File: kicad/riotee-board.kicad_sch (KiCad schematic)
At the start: 0 parts

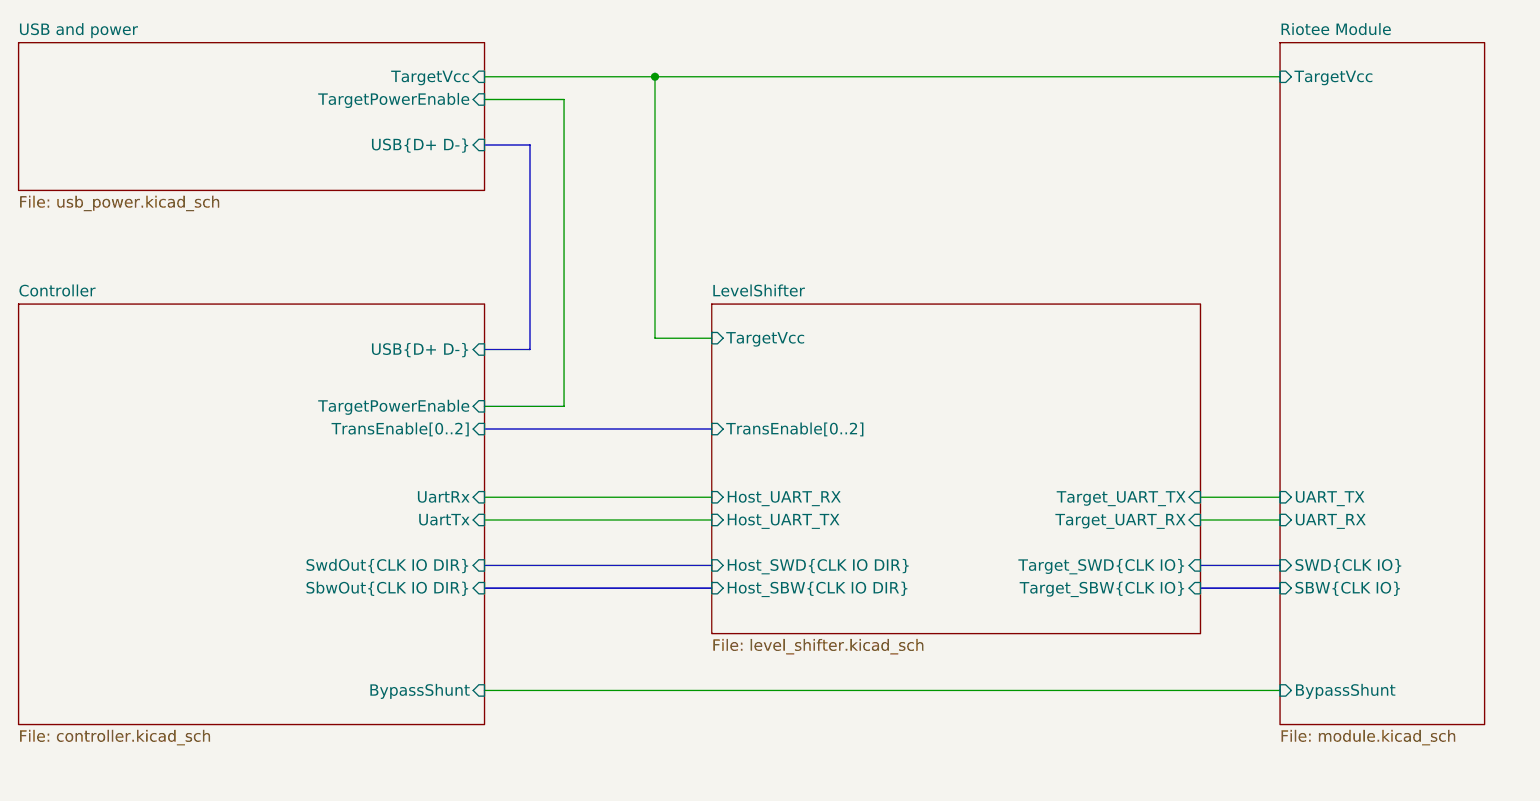
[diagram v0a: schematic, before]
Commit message: add fourth level converter for simultaneous programming + TX/RX
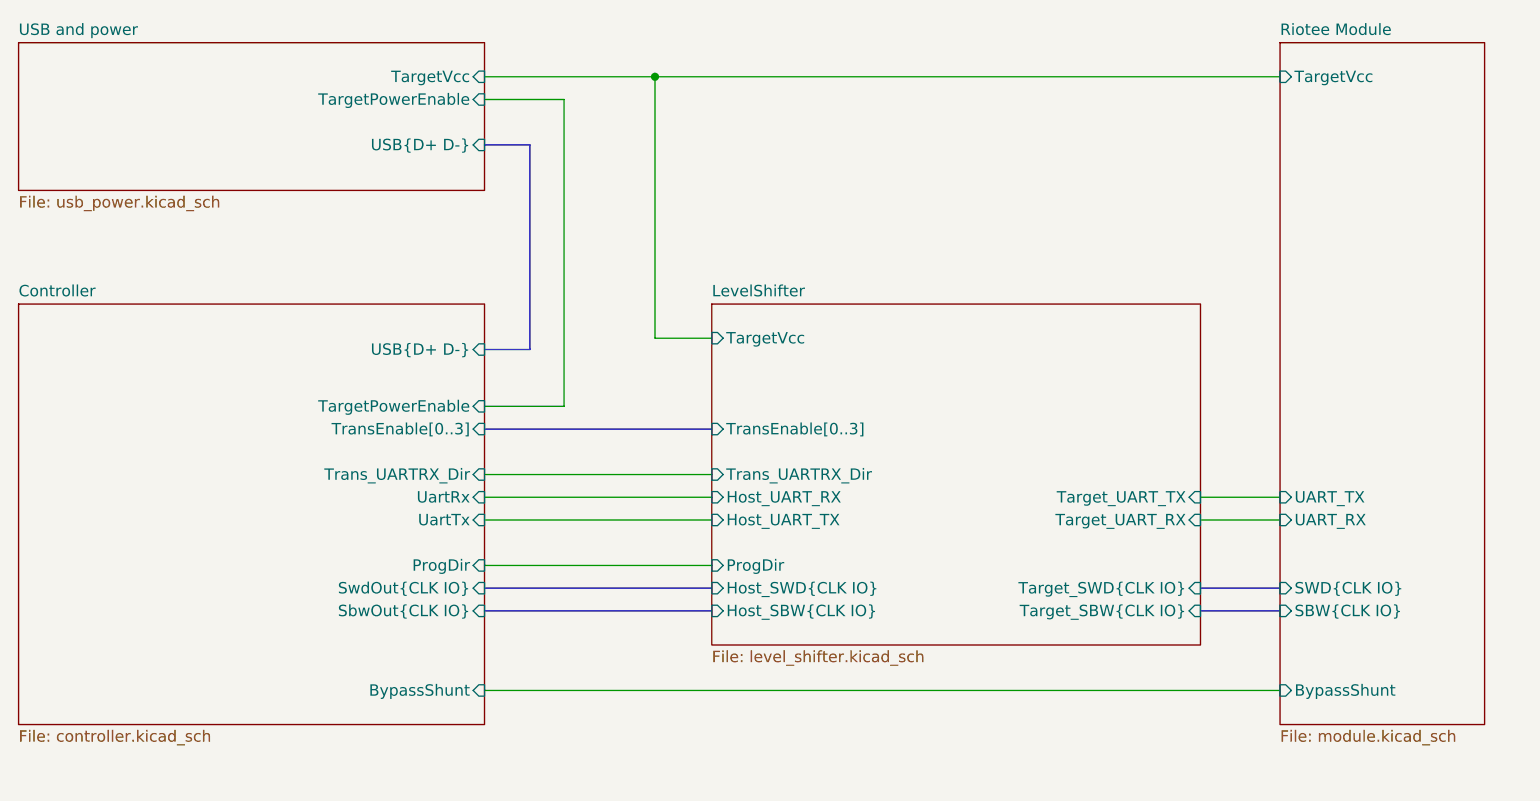
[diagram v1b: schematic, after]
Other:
- sheet Controller ports: added ProgDir, SbwOut{CLK IO}, SwdOut{CLK IO}, TransEnable[0..3], Trans_UARTRX_Dir; removed SbwOut{CLK IO DIR}, SwdOut{CLK IO DIR}, TransEnable[0..2]
- sheet LevelShifter ports: added Host_SBW{CLK IO}, Host_SWD{CLK IO}, ProgDir, TransEnable[0..3], Trans_UARTRX_Dir; removed Host_SBW{CLK IO DIR}, Host_SWD{CLK IO DIR}, TransEnable[0..2]

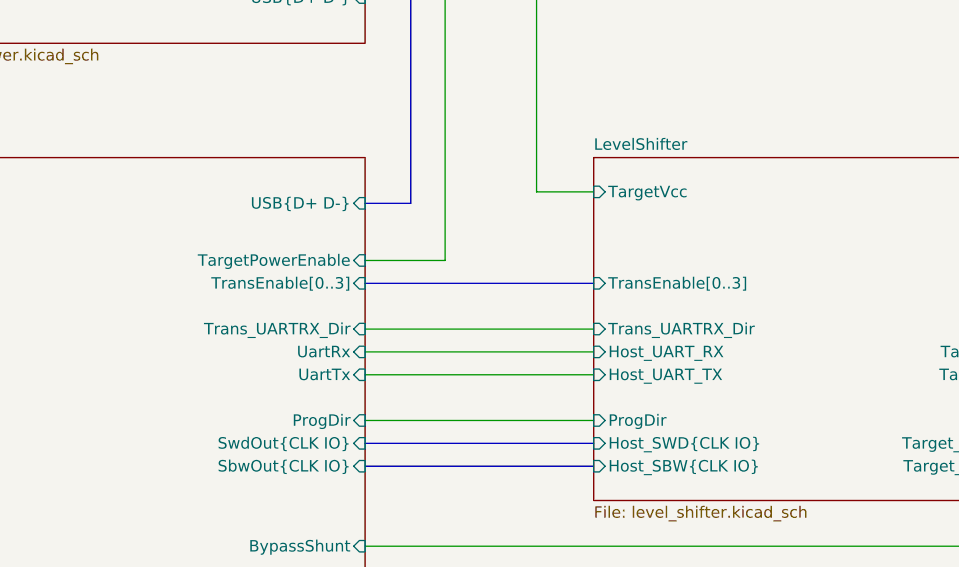
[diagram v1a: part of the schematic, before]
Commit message: fix some net names
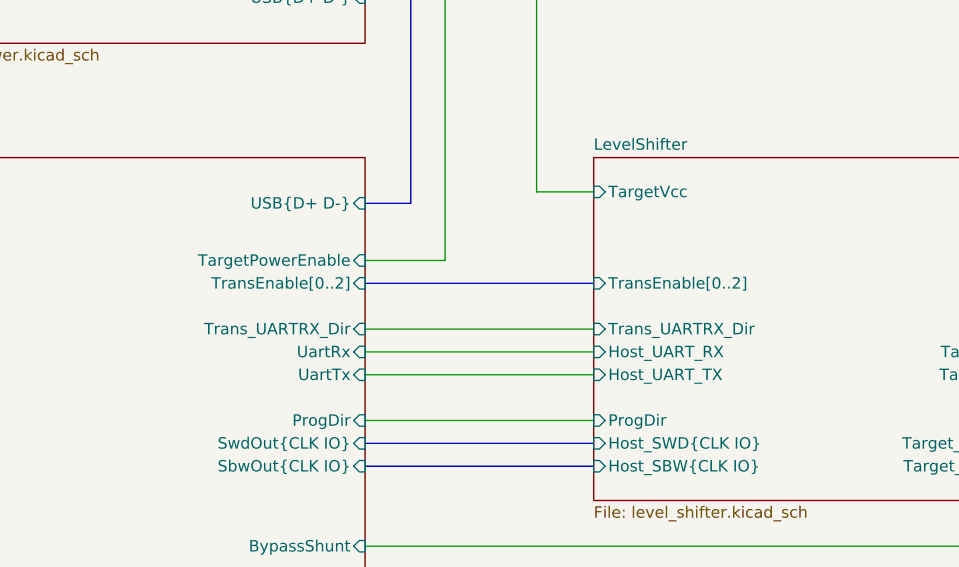
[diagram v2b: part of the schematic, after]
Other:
- sheet Controller ports: added TransEnable[0..2]; removed TransEnable[0..3]
- sheet LevelShifter ports: added TransEnable[0..2]; removed TransEnable[0..3]
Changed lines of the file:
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@@
       (effects (font (size 1.27 1.27)) (justify right))
     )
-    (pin "TransEnable[0..3]" input (at 114.3 104.14 0)
+    (pin "TransEnable[0..2]" input (at 114.3 104.14 0)
       (effects (font (size 1.27 1.27)) (justify right))
     )
@@
       (effects (font (size 1.27 1.27)) (justify left))
     )
-    (pin "TransEnable[0..3]" input (at 139.7 104.14 180)
+    (pin "TransEnable[0..2]" input (at 139.7 104.14 180)
       (effects (font (size 1.27 1.27)) (justify left))
     )

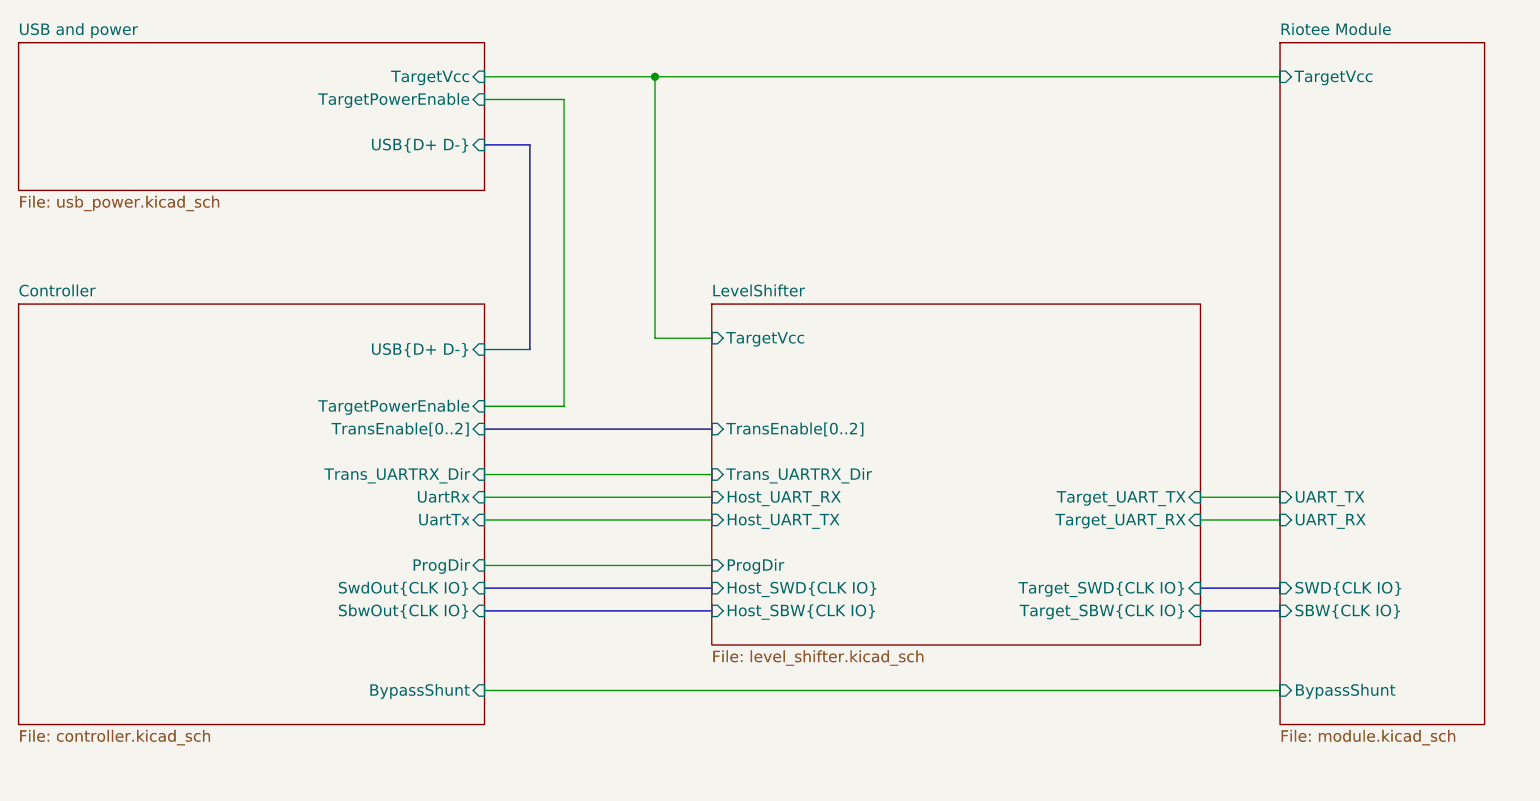
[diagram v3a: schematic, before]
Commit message: replace target supply diode with analog switch
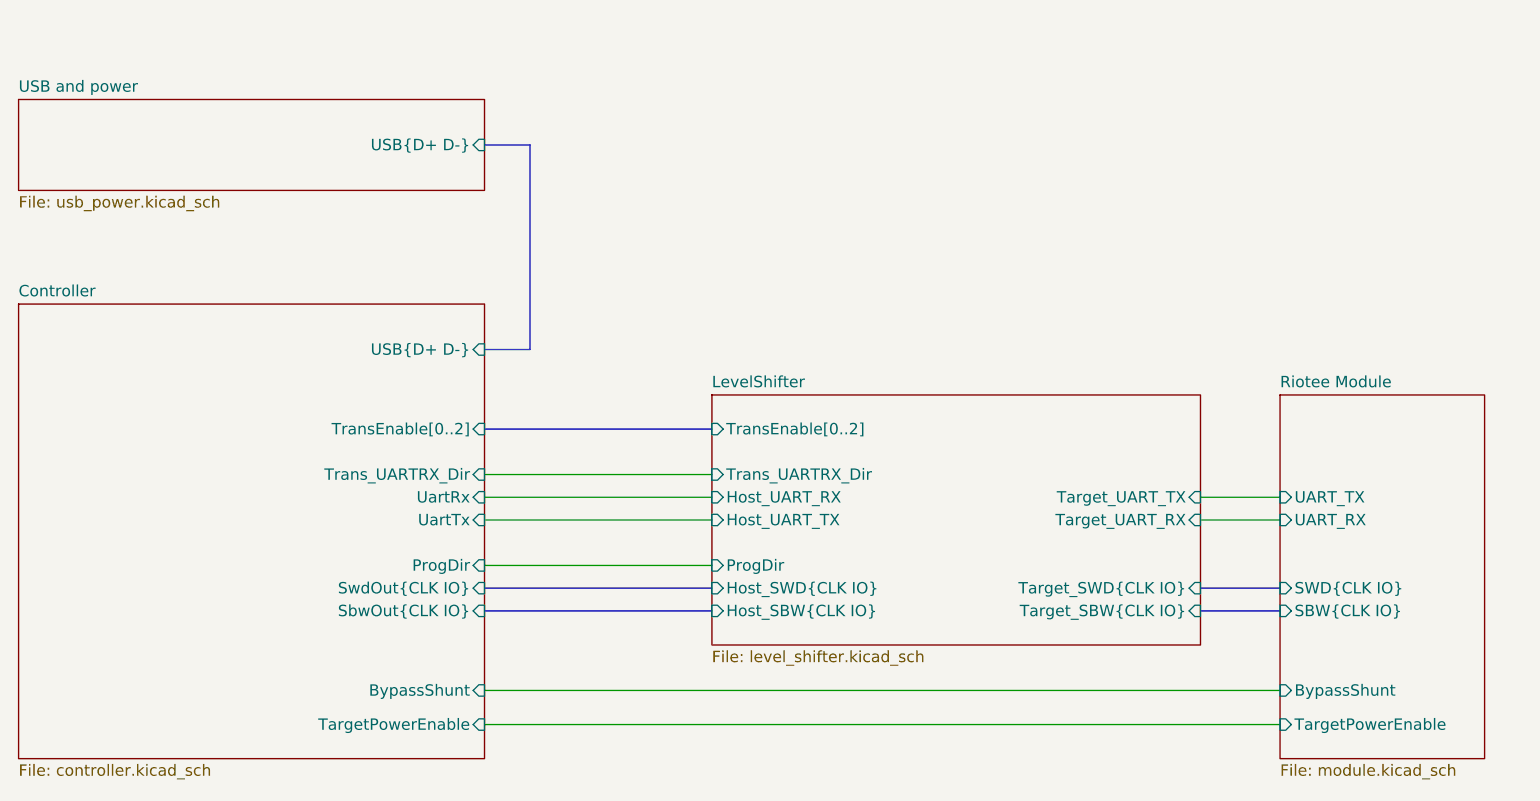
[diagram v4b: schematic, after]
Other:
- sheet LevelShifter ports: added none; removed TargetVcc
- sheet Riotee Module ports: added TargetPowerEnable; removed TargetVcc
- sheet USB and power ports: added none; removed TargetPowerEnable, TargetVcc
